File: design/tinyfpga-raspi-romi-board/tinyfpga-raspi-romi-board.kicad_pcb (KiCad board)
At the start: 2 copper layers, 72 parts, among them J1 TINYFPGA_J1, J10 ROMI_ENC_LEFT, J11 ROMI_ENC_RIGHT, J12 QTR_LEFT, J13 QTR_RIGHT, J14 SONAR_LEFT, J15 SONAR_RIGHT, J16 PWR_SEL1, J17 PWR_SEL0, J18 RPI_EXTRA, J19 ON_OFF, J2 TINYFPGA_J2, J20 ROMI_POWER, J3 Raspberry_Pi_2_3, J4 TINYFPGA_J4, J5 TINYFPGA_J5, J6 WP_JUMP, J7 ROMI_VSW, J8 FUSE_JUMP, J9 ROMI_MOTOR_DRIVE, Q1 2N7000, Q2 2N7000, Q3 2N7000, Q4 2N7000, Q5 2N7000, Q6 2N7000, Q7 2N7000, Q8 2N7000, SW2 SW_Push, SW3 SW_Push, SW4 SW_Push, U1 CAT24C128

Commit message: imported mech drawings to kicad pcb for placement
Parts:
- J20, J7, J9: moved to B.Cu
- moved J10 366.9 mm to (-242.3, 134.9)
- moved J11 366.9 mm to (-247.4, 134.9)
- moved A1 289.4 mm to (-88.6, 10.4)
- moved C1 289.4 mm to (-92.5, 20.6)
- moved C2 289.4 mm to (-78.5, 1.52)
- moved D1 289.4 mm to (-77.2, 10.4)
- moved F1 289.4 mm to (-79.8, 19.3)
- moved J12 289.4 mm to (-185.2, 147.6)
- moved J13 289.4 mm to (-177.5, 147.6)
- moved J16 289.4 mm to (-88.6, 127.3)
- moved J17 289.4 mm to (-82.3, 127.3)
- moved J18 289.4 mm to (-224.5, -23.9)
- moved J19 289.4 mm to (-97.5, 13.0)
- moved J6 289.4 mm to (-204.2, 43.4)
- moved J8 289.4 mm to (-81.0, 26.9)
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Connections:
- J20 pad 1: /RPI_GPIO26 -> (no net)
- J20 pad 10: GND -> (no net)
- J20 pad 2: GND -> (no net)
- J20 pad 3: /RPI_GPIO24 -> (no net)
- J20 pad 4: GND -> (no net)
- J20 pad 5: /ROMI_3V3 -> (no net)
- J20 pad 6: GND -> (no net)
- J20 pad 7: /ROMI_3V3 -> (no net)
- J20 pad 8: GND -> (no net)
- J20 pad 9: /ROMI_3V3 -> (no net)
- J7 pad 1: +BATT -> (no net)
- J7 pad 2: GND -> (no net)
- J7 pad 3: +BATT -> (no net)
- J7 pad 4: GND -> (no net)
- J7 pad 5: +BATT -> (no net)
- J7 pad 6: GND -> (no net)
- J9 pad 1: /ROMI_~SLPL -> (no net)
- J9 pad 2: /ROMI_DIRL -> (no net)
- J9 pad 3: /ROMI_PWML -> (no net)
- J9 pad 4: /ROMI_~SLPR -> (no net)
- J9 pad 5: /ROMI_DIRR -> (no net)
- J9 pad 6: /ROMI_PWMR -> (no net)
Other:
- board outline added: 76.4 x 114.8 mm
- net class Default: clearance 0.2 -> 0.2032; trace_width 0.25 -> 0.254
- rule trace_clearance: 0.2 -> 0.2032

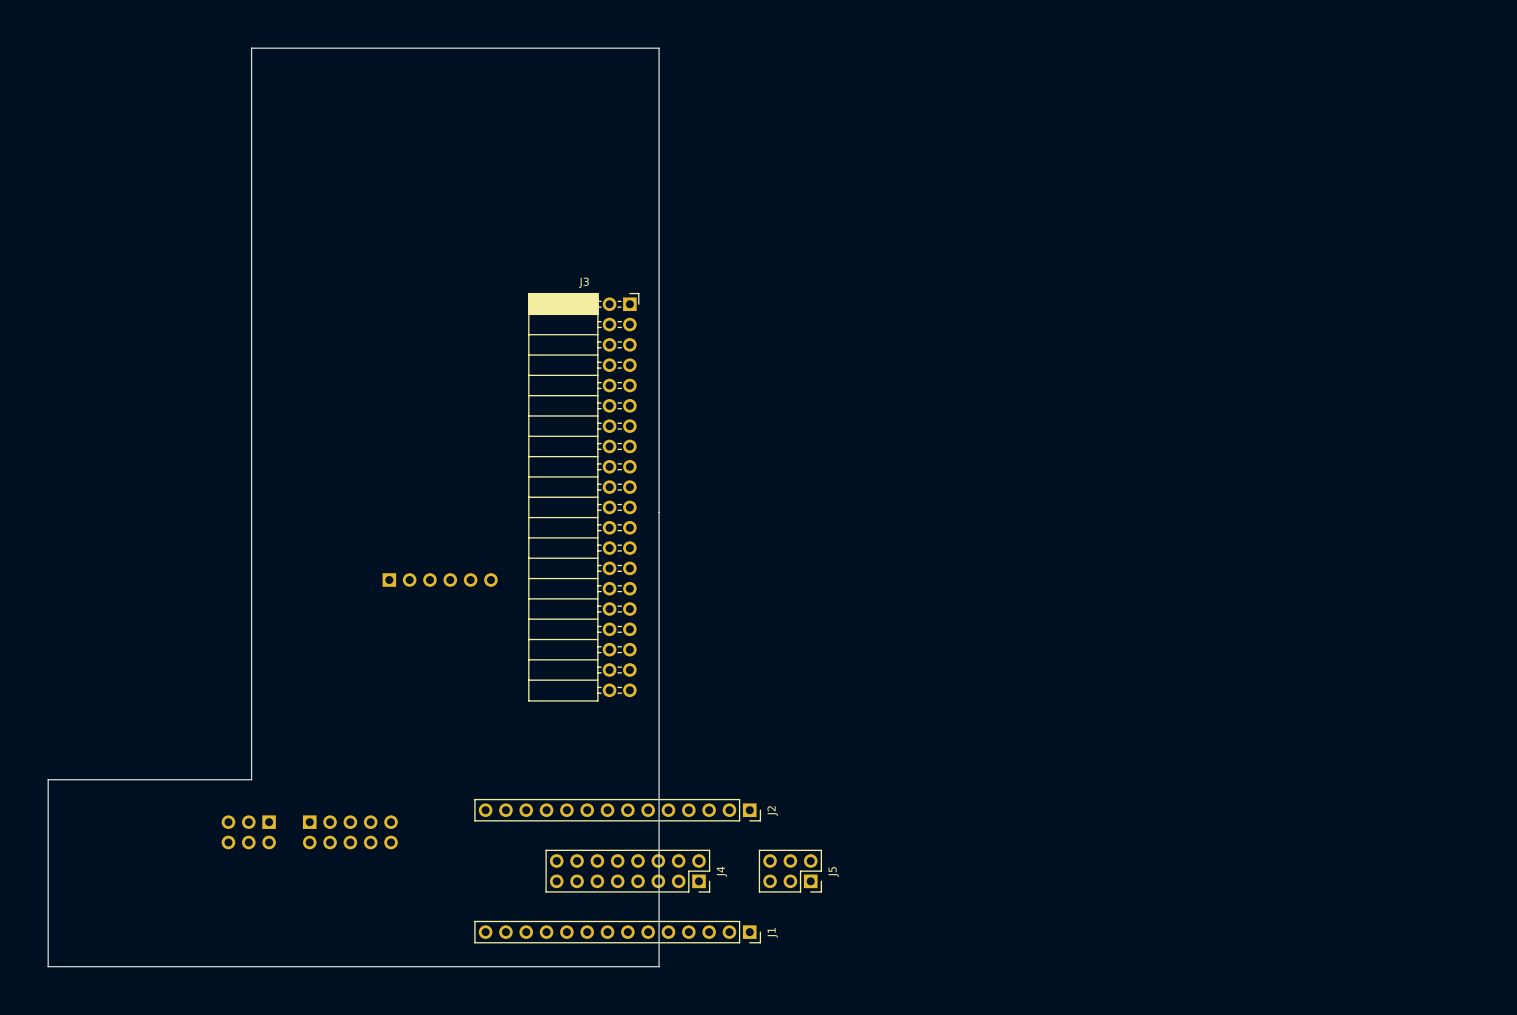
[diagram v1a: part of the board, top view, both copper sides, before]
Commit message: made some minor tweaks and measured tinypcb with headers
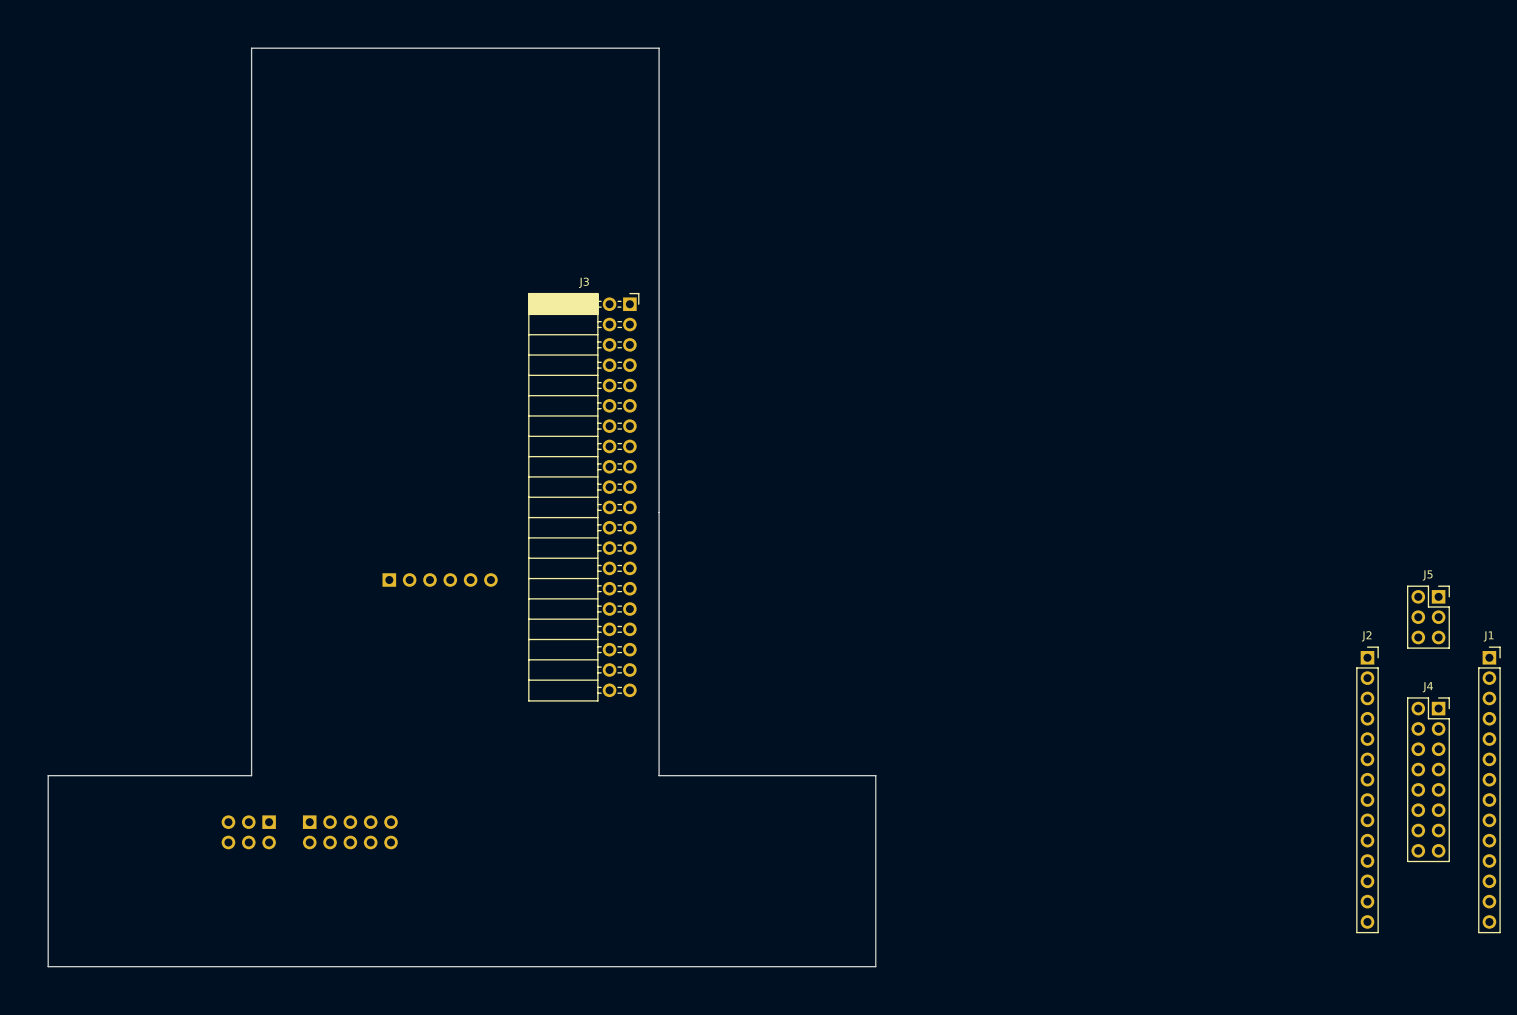
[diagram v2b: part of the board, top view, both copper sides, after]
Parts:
- moved J1 98.6 mm to (232.9, 104.6), turned to 0 degrees
- moved J4 94.9 mm to (226.6, 111.0), turned to 0 degrees
- moved J5 86.2 mm to (226.6, 97.0), turned to 0 degrees
- moved J2 79.5 mm to (217.7, 104.6), turned to 0 degrees
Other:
- board size 76.4 x 114.8 mm -> 103.4 x 114.8 mm

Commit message: Everything fits on a board
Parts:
- J14: footprint Connector_PinHeader_2.54mm:PinHeader_1x04_P2.54mm_Vertical -> Connector_PinSocket_2.54mm:PinSocket_1x04_P2.54mm_Vertical
- J18: footprint Connector_PinHeader_2.54mm:PinHeader_2x09_P2.54mm_Vertical -> Connector_PinHeader_2.54mm:PinHeader_1x18_P2.54mm_Vertical
- J19, J6, J8: footprint Connector_PinHeader_1.27mm:PinHeader_1x02_P1.27mm_Vertical -> Connector_PinHeader_2.54mm:PinHeader_1x02_P2.54mm_Vertical
- J20: footprint Connector_PinHeader_2.54mm:PinHeader_2x05_P2.54mm_Vertical -> Connector_PinHeader_2.54mm:PinHeader_2x05_P2.54mm_Vertical_SMD
- J4: footprint Connector_PinSocket_2.54mm:PinSocket_2x08_P2.54mm_Vertical -> Connector_PinSocket_2.54mm:PinSocket_2x08_P2.54mm_Vertical_SMD
- J5, J7: footprint Connector_PinSocket_2.54mm:PinSocket_2x03_P2.54mm_Vertical -> Connector_PinSocket_2.54mm:PinSocket_2x03_P2.54mm_Vertical_SMD
- J9: footprint Connector_PinHeader_2.54mm:PinHeader_1x06_P2.54mm_Vertical -> Connector_PinHeader_2.54mm:PinHeader_1x06_P2.54mm_Vertical_SMD_Pin1Left
- moved J11 377.5 mm to (127.6, 92.1)
- moved J18 369.4 mm to (107.3, 138.4), turned to 90 degrees
- moved R22 355.0 mm to (133.0, 125.3)
- moved J6 354.5 mm to (140.0, 128.5)
- moved R1 354.5 mm to (147.6, 127.3)
- moved R2 354.5 mm to (138.7, 123.4)
- moved U1 353.1 mm to (130.2, 130.8)
- moved J13 329.4 mm to (130.8, 31.6), turned to 315 degrees
- moved J10 325.2 mm to (80.0, 92.1)
- moved J12 289.6 mm to (79.4, 29.8), turned to 45 degrees
- moved A1 228.2 mm to (111.4, 120.3)
- moved C1 228.2 mm to (107.6, 130.4)
- moved C2 228.2 mm to (121.5, 111.4)
- moved R4 228.2 mm to (112.6, 112.6)
- moved D1 228.2 mm to (122.8, 120.3)
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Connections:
- J18 pad 1: /RPI_GPIO2 -> /RPI_GPIO3
- J18 pad 10: /RPI_GPIO19 -> /RPI_GPIO18
- J18 pad 11: /RPI_GPIO20 -> /RPI_GPIO21
- J18 pad 12: /RPI_GPIO21 -> /RPI_GPIO20
- J18 pad 13: /RPI_GPIO22 -> /RPI_GPIO23
- J18 pad 14: /RPI_GPIO23 -> /RPI_GPIO22
- J18 pad 2: /RPI_GPIO3 -> /RPI_GPIO2
- J18 pad 3: /RPI_GPIO4 -> /RPI_GPIO7
- J18 pad 4: /RPI_GPIO7 -> /RPI_GPIO4
- J18 pad 5: /RPI_GPIO12 -> /RPI_GPIO13
- J18 pad 6: /RPI_GPIO13 -> /RPI_GPIO12
- J18 pad 7: /RPI_GPIO16 -> /RPI_GPIO17
- J18 pad 8: /RPI_GPIO17 -> /RPI_GPIO16
- J18 pad 9: /RPI_GPIO18 -> /RPI_GPIO19
- J20 pad 1: (no net) -> /RPI_GPIO26
- J20 pad 10: (no net) -> GND
- J20 pad 2: (no net) -> GND
- J20 pad 3: (no net) -> /RPI_GPIO24
- J20 pad 4: (no net) -> GND
- J20 pad 5: (no net) -> /ROMI_3V3
- J20 pad 6: (no net) -> GND
- J20 pad 7: (no net) -> /ROMI_3V3
- J20 pad 8: (no net) -> GND
- J20 pad 9: (no net) -> /ROMI_3V3
- J5 pad 1: /FPGA_CLK -> (no net)
- J5 pad 3: /FPGA_LED -> (no net)
- J5 pad 4: /FPGA_USB_PU -> (no net)
- J5 pad 5: /FPGA_USB_P -> (no net)
- J5 pad 6: /FPGA_USB_N -> (no net)
- J7 pad 1: (no net) -> +BATT
- J7 pad 2: (no net) -> GND
- J7 pad 3: (no net) -> +BATT
- J7 pad 4: (no net) -> GND
- J7 pad 5: (no net) -> +BATT
- J7 pad 6: (no net) -> GND
- J9 pad 1: (no net) -> /ROMI_~SLPL
- J9 pad 2: (no net) -> /ROMI_DIRL
- J9 pad 3: (no net) -> /ROMI_PWML
- J9 pad 4: (no net) -> /ROMI_~SLPR
- J9 pad 5: (no net) -> /ROMI_DIRR
- J9 pad 6: (no net) -> /ROMI_PWMR
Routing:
- net +5V: track 82.4 -> 31.6 mm
- net Net-(D6-Pad2): track 15.0 -> 6.13 mm
- net /FPGA_BTN_RST: track 12.9 -> 6.50 mm
- net /FPGA_BTN1: track 12.7 -> 6.35 mm
- net /FPGA_BTN0: track 12.9 -> 6.50 mm
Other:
- board size 103.4 x 114.8 mm -> 103.4 x 121.3 mm

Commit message: All components placed on board. Needs routing doe
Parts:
- moved C1 18.9 mm to (123.8, 120.7), turned to 90 degrees
- moved C2 17.4 mm to (117.5, 128.3), turned to 90 degrees
- moved R22 14.4 mm to (147.3, 126.4), turned to 0 degrees
- moved J9 12.8 mm to (102.0, 107.6)
- moved J19 12.6 mm to (111.8, 114.3), turned to 90 degrees
- moved U1 11.5 mm to (141.6, 129.5)
- moved R2 10.2 mm to (147.3, 128.9)
- moved F1 8.78 mm to (111.8, 127.0), turned to 90 degrees
- moved J8 7.65 mm to (106.7, 128.3), turned to 180 degrees
- moved D1 6.76 mm to (125.7, 126.4)
- moved R23 6.13 mm to (118.2, 43.7), turned to 45 degrees
- moved J4 5.25 mm to (111.8, 89.5)
- moved R4 5.10 mm to (117.5, 114.3)
- moved J6 5.00 mm to (142.9, 124.5), turned to 270 degrees
- moved J2 4.49 mm to (87.6, 98.4)
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
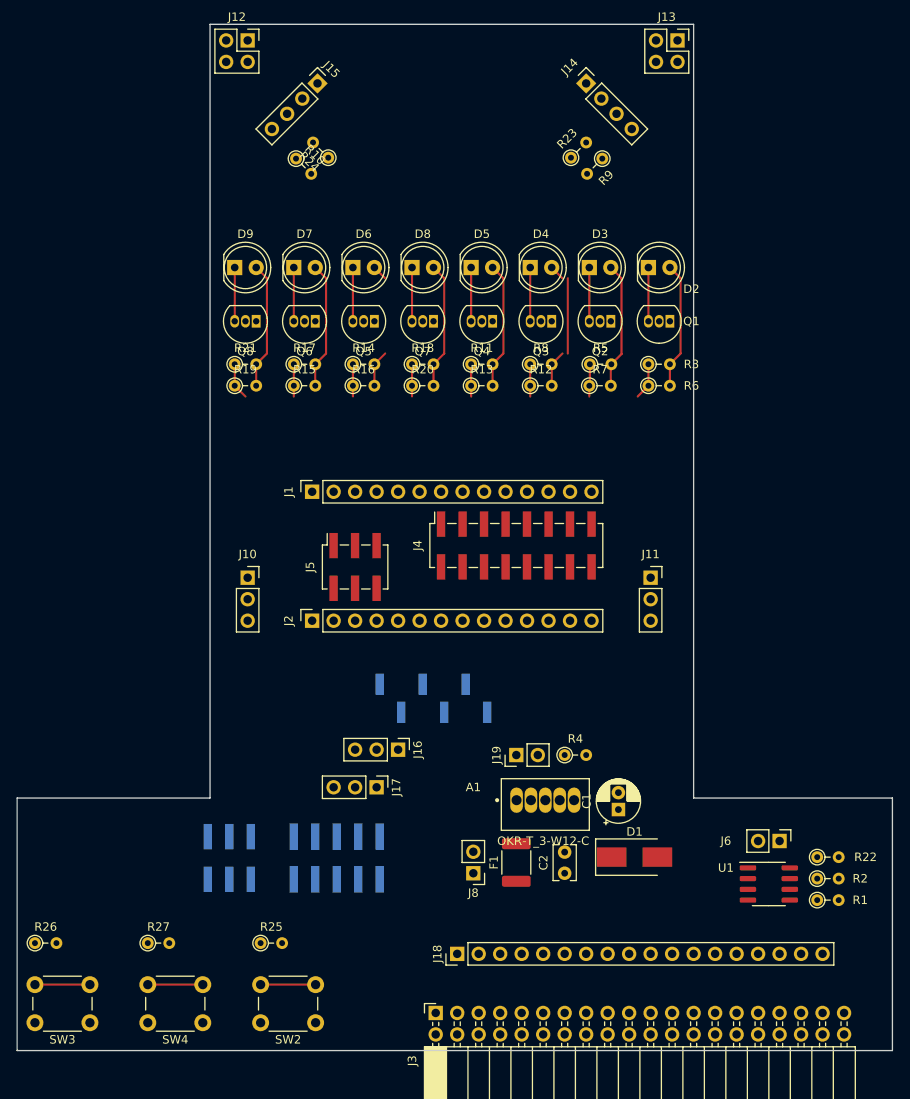
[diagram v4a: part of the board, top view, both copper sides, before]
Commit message: Spaced out componenets more
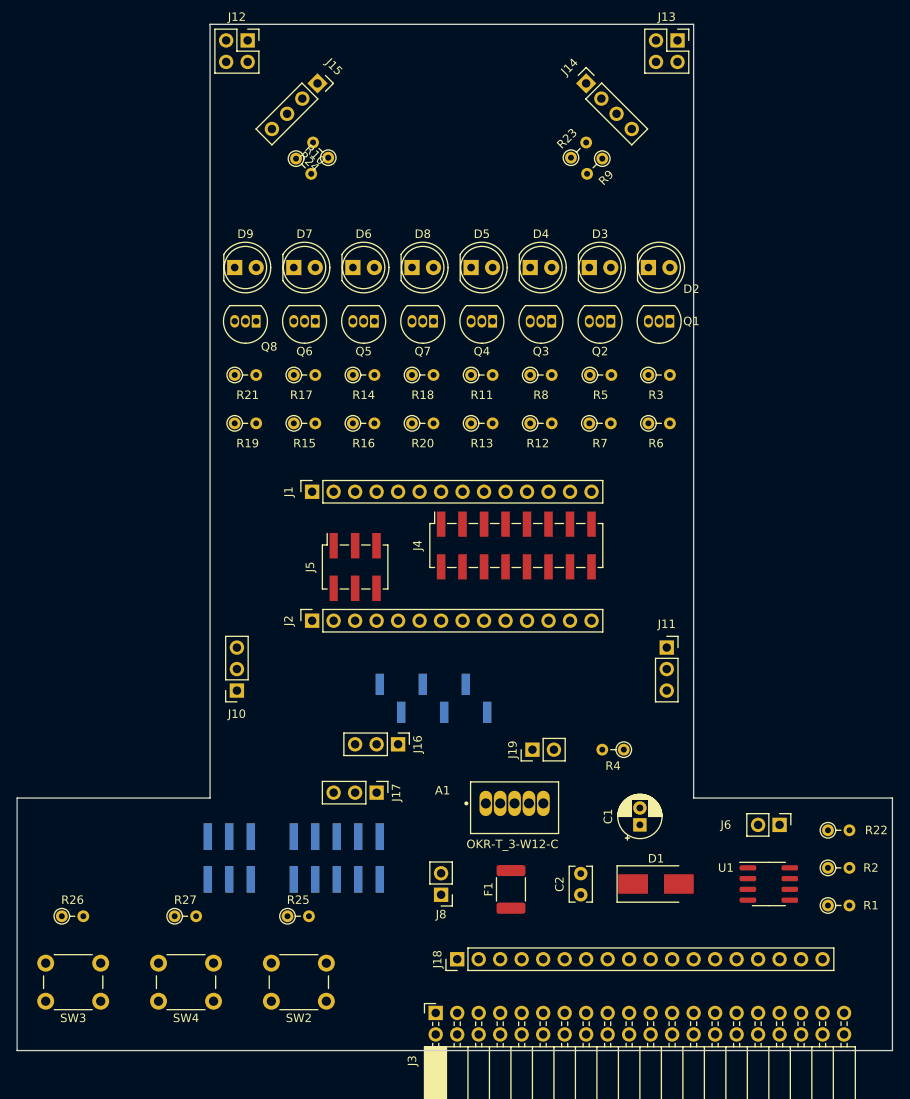
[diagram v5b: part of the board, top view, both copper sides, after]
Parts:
- J15: footprint Connector_PinHeader_2.54mm:PinHeader_1x04_P2.54mm_Vertical -> Connector_PinSocket_2.54mm:PinSocket_1x04_P2.54mm_Vertical
- J7: footprint Connector_PinSocket_2.54mm:PinSocket_2x03_P2.54mm_Vertical_SMD -> Connector_PinHeader_2.54mm:PinHeader_2x03_P2.54mm_Vertical_SMD
- moved J10 13.4 mm to (78.7, 106.7), turned to 180 degrees
- moved J11 8.47 mm to (129.5, 101.6)
- moved R4 7.01 mm to (124.5, 113.7), turned to 180 degrees
- moved J8 4.58 mm to (102.9, 130.8)
- moved R25 4.49 mm to (84.7, 133.3)
- moved R26 4.49 mm to (58.0, 133.3)
- moved R27 4.49 mm to (71.4, 133.3)
- moved R12 4.44 mm to (113.4, 75.1)
- moved R13 4.44 mm to (106.4, 75.1)
- moved R15 4.44 mm to (85.5, 75.1)
- moved R16 4.44 mm to (92.4, 75.1)
- moved R19 4.44 mm to (78.5, 75.1)
- moved R20 4.44 mm to (99.4, 75.1)
- moved R6 4.44 mm to (127.4, 75.1)
- moved R7 4.44 mm to (120.4, 75.1)
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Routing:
- net +5V: track 31.6 -> 0.00 mm
- net Net-(D9-Pad2): track 15.0 -> 0.00 mm
- net Net-(D2-Pad2): track 15.0 -> 0.00 mm
- net Net-(D8-Pad2): track 15.0 -> 0.00 mm
- net Net-(D7-Pad2): track 15.0 -> 0.00 mm
- net Net-(D5-Pad2): track 15.0 -> 0.00 mm
- net Net-(D4-Pad2): track 15.0 -> 0.00 mm
- net Net-(D3-Pad2): track 15.0 -> 0.09 mm
- net /FPGA_BTN_RST: track 6.50 -> 0.00 mm
- net /FPGA_BTN0: track 6.50 -> 0.00 mm
- net Net-(D9-Pad1): track 6.35 -> 0.00 mm
- net Net-(D8-Pad1): track 6.35 -> 0.00 mm
- net Net-(D7-Pad1): track 6.35 -> 0.00 mm
- net Net-(D6-Pad1): track 6.35 -> 0.00 mm
- net Net-(D5-Pad1): track 6.35 -> 0.00 mm
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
